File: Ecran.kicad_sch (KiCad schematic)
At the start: 0 parts

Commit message: Test ajout de composant depuis l'internet
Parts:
- added U3: 8205A, 8205A:SOT95P285X140-6N, symbol 8205A:8205A
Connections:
- new net: U3.2, U3.5
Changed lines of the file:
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@@
 	(generator_version "9.0")
 	(paper "A4")
+	(symbol
+		(lib_id "8205A:8205A")
+		(at 81.28 81.28 0)
+		(unit 1)
+		(exclude_from_sim no)
+		(in_bom yes)
+		(on_board yes)
+		(dnp no)
+		(fields_autoplaced yes)
+		(property "Reference" "U3"
+			(at 90.17 79.0828 0)
+			(effects
+				(font
+					(size 1.27 1.27)
+				)
+				(justify left)
+			)
+		)
+		(property "Value" "8205A"
+			(at 90.17 81.6228 0)
+			(effects
+				(font
+					(size 1.27 1.27)
+				)
+				(justify left)
+			)
+		)
+		(property "Footprint" "8205A:SOT95P285X140-6N"
+			(at 81.28 81.28 0)
+			(effects
+				(font
+					(size 1.27 1.27)
+				)
+				(justify bottom)
+				(hide yes)
+			)
+		)
+		(property "Datasheet" ""
+			(at 81.28 81.28 0)
+			(effects
+				(font
+					(size 1.27 1.27)
+				)
+				(hide yes)
+			)
+		)
+		(property "Description" ""
+			(at 81.28 81.28 0)
+			(effects
+				(font
+					(size 1.27 1.27)
+				)
+				(hide yes)
+			)
+		)
+		(property "MF" "UMW"
+			(at 81.28 81.28 0)
+			(effects
+				(font
+					(size 1.27 1.27)
+				)
+				(justify bottom)
+				(hide yes)
+			)
+		)
+		(property "MAXIMUM_PACKAGE_HEIGHT" "1.40mm"
+			(at 81.28 81.28 0)
+			(effects
+				(font
+					(size 1.27 1.27)
+				)
+				(justify bottom)
+				(hide yes)
+			)
+		)
+		(property "Package" "SOT-23-6 UMW"
+			(at 81.28 81.28 0)
+			(effects
+				(font
+					(size 1.27 1.27)
+				)
+				(justify bottom)
+				(hide yes)
+			)
+		)
+		(property "Price" "None"
+			(at 81.28 81.28 0)
+			(effects
+				(font
+					(size 1.27 1.27)
+				)
+				(justify bottom)
+				(hide yes)
+			)
+		)
+		(property "Check_prices" "https://www.snapeda.com/parts/8205A/UMW/view-part/?ref=eda"
+			(at 81.28 81.28 0)
+			(effects
+				(font
+					(size 1.27 1.27)
+				)
+				(justify bottom)
+				(hide yes)
+			)
+		)
+		(property "STANDARD" "IPC 7351B"
+			(at 81.28 81.28 0)
+			(effects
+				(font
+					(size 1.27 1.27)
+				)
+				(justify bottom)
+				(hide yes)
+			)
+		)
+		(property "PARTREV" "NA"
+			(at 81.28 81.28 0)
+			(effects
+				(font
+					(size 1.27 1.27)
+				)
+				(justify bottom)
+				(hide yes)
+			)
+		)
+		(property "SnapEDA_Link" "https://www.snapeda.com/parts/8205A/UMW/view-part/?ref=snap"
+			(at 81.28 81.28 0)
+			(effects
+				(font
+					(size 1.27 1.27)
+				)
+				(justify bottom)
+				(hide yes)
+			)
+		)
+		(property "MP" "8205A"
+			(at 81.28 81.28 0)
+			(effects
+				(font
+					(size 1.27 1.27)
+				)
+				(justify bottom)
+				(hide yes)
+			)
+		)
+		(property "Description_1" "Mosfet Array 20V 5A 830mW (Ta) Surface Mount SOT-23-6"
+			(at 81.28 81.28 0)
+			(effects
+				(font
+					(size 1.27 1.27)
+				)
+				(justify bottom)
+				(hide yes)
+			)
+		)
+		(property "Availability" "In Stock"
+			(at 81.28 81.28 0)
+			(effects
+				(font
+					(size 1.27 1.27)
+				)
+				(justify bottom)
+				(hide yes)
+			)
+		)
+		(property "MANUFACTURER" "UMW"
+			(at 81.28 81.28 0)
+			(effects
+				(font
+					(size 1.27 1.27)
+				)
+				(justify bottom)
+				(hide yes)
+			)
+		)
+		(pin "6"
+		)
+		(pin "3"
+		)
+		(pin "1"
+		)
+		(pin "4"
+		)
+		(pin "2"
+		)
+		(pin "5"
+		)
+		(instances
+			(project ""
+				(path "/90bd0b60-6e70-43e1-8410-99fb54688c17/3922ef04-1be0-4a1a-a432-baea08402c76"
+					(reference "U3")
+					(unit 1)
+				)
+			)
+		)
+	)
 )

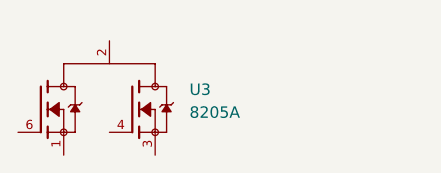
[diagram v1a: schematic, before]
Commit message: Correction capteur + ajout composant
Il fallait changer le nom dans le gestionnaire de footprint
Correction de la connectique du capteur, mais à vérifier quand même
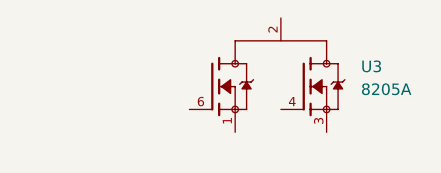
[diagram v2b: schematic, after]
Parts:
- U3: footprint 8205A:SOT95P285X140-6N -> Composants_Perso:SOT95P285X140-6N
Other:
- moved on the sheet: U3
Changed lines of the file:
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@@
 	(symbol
 		(lib_id "8205A:8205A")
-		(at 81.28 81.28 0)
+		(at 100.33 78.74 0)
 		(unit 1)
 		(exclude_from_sim no)
@@
 		(fields_autoplaced yes)
 		(property "Reference" "U3"
-			(at 90.17 79.0828 0)
+			(at 109.22 76.5428 0)
 			(effects
 				(font
@@
 		)
 		(property "Value" "8205A"
-			(at 90.17 81.6228 0)
+			(at 109.22 79.0828 0)
 			(effects
 				(font
@@
 			)
 		)
-		(property "Footprint" "8205A:SOT95P285X140-6N"
-			(at 81.28 81.28 0)
+		(property "Footprint" "Composants_Perso:SOT95P285X140-6N"
+			(at 100.33 78.74 0)
 			(effects
 				(font
@@
 		)
 		(property "Datasheet" ""
-			(at 81.28 81.28 0)
+			(at 100.33 78.74 0)
 			(effects
 				(font
@@
 		)
 		(property "Description" ""
-			(at 81.28 81.28 0)
+			(at 100.33 78.74 0)
 			(effects
 				(font
@@
 		)
 		(property "MF" "UMW"
-			(at 81.28 81.28 0)
+			(at 100.33 78.74 0)
 			(effects
 				(font
@@
 		)
 		(property "MAXIMUM_PACKAGE_HEIGHT" "1.40mm"
-			(at 81.28 81.28 0)
+			(at 100.33 78.74 0)
 			(effects
 				(font
@@
 		)
 		(property "Package" "SOT-23-6 UMW"
-			(at 81.28 81.28 0)
+			(at 100.33 78.74 0)
 			(effects
 				(font
@@
 		)
 		(property "Price" "None"
-			(at 81.28 81.28 0)
+			(at 100.33 78.74 0)
 			(effects
 				(font
@@
 		)
 		(property "Check_prices" "https://www.snapeda.com/parts/8205A/UMW/view-part/?ref=eda"
-			(at 81.28 81.28 0)
+			(at 100.33 78.74 0)
 			(effects
 				(font
@@
 		)
 		(property "STANDARD" "IPC 7351B"
-			(at 81.28 81.28 0)
+			(at 100.33 78.74 0)
 			(effects
 				(font
@@
 		)
 		(property "PARTREV" "NA"
-			(at 81.28 81.28 0)
+			(at 100.33 78.74 0)
 			(effects
 				(font
@@
 		)
 		(property "SnapEDA_Link" "https://www.snapeda.com/parts/8205A/UMW/view-part/?ref=snap"
-			(at 81.28 81.28 0)
+			(at 100.33 78.74 0)
 			(effects
 				(font
@@
 		)
 		(property "MP" "8205A"
-			(at 81.28 81.28 0)
+			(at 100.33 78.74 0)
 			(effects
 				(font
@@
 		)
 		(property "Description_1" "Mosfet Array 20V 5A 830mW (Ta) Surface Mount SOT-23-6"
-			(at 81.28 81.28 0)
+			(at 100.33 78.74 0)
 			(effects
 				(font
@@
 		)
 		(property "Availability" "In Stock"
-			(at 81.28 81.28 0)
+			(at 100.33 78.74 0)
 			(effects
 				(font
@@
 		)
 		(property "MANUFACTURER" "UMW"
-			(at 81.28 81.28 0)
+			(at 100.33 78.74 0)
 			(effects
 				(font

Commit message: Partie écran
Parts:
- removed U3: 8205A, Composants_Perso:SOT95P285X140-6N, symbol 8205A:8205A
- added C10, C11, C12, C14, C6, C7, C8, C9: 1uF/50V, symbol Device:C_Small
- added C3, C4: 4.7uF/25V, symbol Device:C
- added C5: 100nF/50V, symbol Device:C
- added D1, D2, D3: MBR0530, Diode_SMD:D_SOD-123, symbol Diode:MBR0530
- added J1: Conn_01x24_Pin, symbol Connector:Conn_01x24_Pin
- added L1: 10u, symbol Device:L
- added Q1: Q_NMOS_GSD, symbol Transistor_FET:Q_NMOS_GSD
- added Q2: Q_NPN_BCE, symbol Transistor_BJT:Q_NPN_BCE
- added R3: 3, symbol Device:R
- added R4: 10K, symbol Device:R
- added R5: 100k, symbol Device:R
- added R6: 10k, symbol Device:R
- added R7: 47K, symbol Device:R
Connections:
- new net: C3.2, D3.2 (A), L1.2, Q1.3 (D)
- new net: C3.1, D1.2 (A), D2.1 (K)
- new net: Q2.1 (B), R5.1, R6.2
- new net: C11.1, J1.24 (Pin_24)
- new net: C10.1, J1.22 (Pin_22)
- new net: C8.1, J1.18 (Pin_18)
- new net: C12.1, J1.5 (Pin_5)
- new net: C14.1, J1.20 (Pin_20)
- new net: Q2.2 (C), R7.1
- new net 3V3_OUT: C4.2, C6.1, J1.15 (Pin_15), J1.16 (Pin_16), L1.1
- new net BS: J1.8 (Pin_8)
- new net EPD PWR: R6.1
- new net EPD_BUSY: J1.9 (Pin_9)
- new net EPD_CS: J1.12 (Pin_12)
- new net EPD_DC: J1.11 (Pin_11)
- new net EPD_DIN: J1.14 (Pin_14)
- new net EPD_RST: J1.10 (Pin_10)
- new net EPD_SCK: J1.13 (Pin_13)
- new net GDR: J1.2 (Pin_2), Q1.1 (G), R4.2
- new net GND: C10.2, C11.2, C12.2, C14.2, C4.1, C5.2, C6.2, C7.2, C8.2, C9.2, D1.1 (K), J1.17 (Pin_17), Q2.3 (E), R3.1, R4.1, R5.2
- new net RESE: J1.3 (Pin_3), Q1.2 (S), R3.2
- new net VCC INT: C5.1, R7.2
- new net VGH: C9.1, D3.1 (K), J1.21 (Pin_21)
- new net VGL: C7.1, D2.2 (A), J1.23 (Pin_23)
- no-connect marks 0 -> 5
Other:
- note added: "Boost Converter"
- note added: "Connecteur"
- note added: "Interrupteur de puissance"

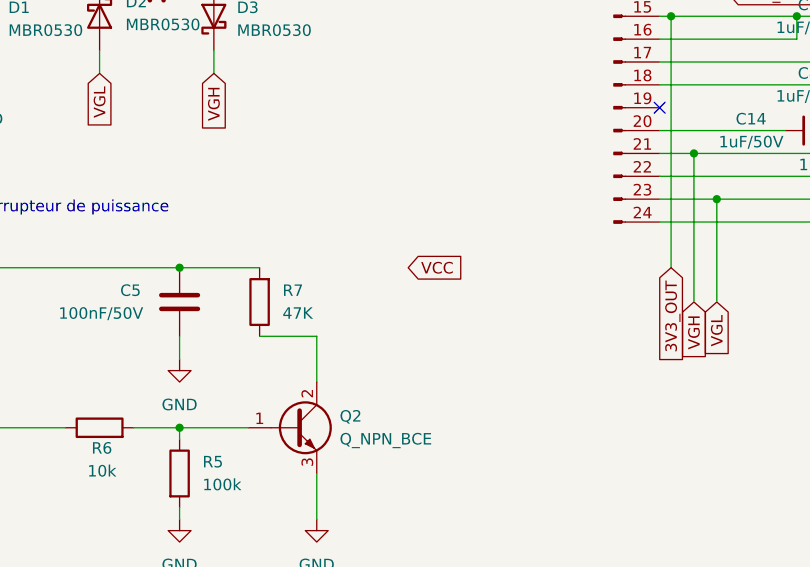
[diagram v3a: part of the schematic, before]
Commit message: Ajout total de la partie alimentation
Ajout de composant depuis un site internet ->OK
Fin de la partie écran et alimentation : ajout de tous les composants
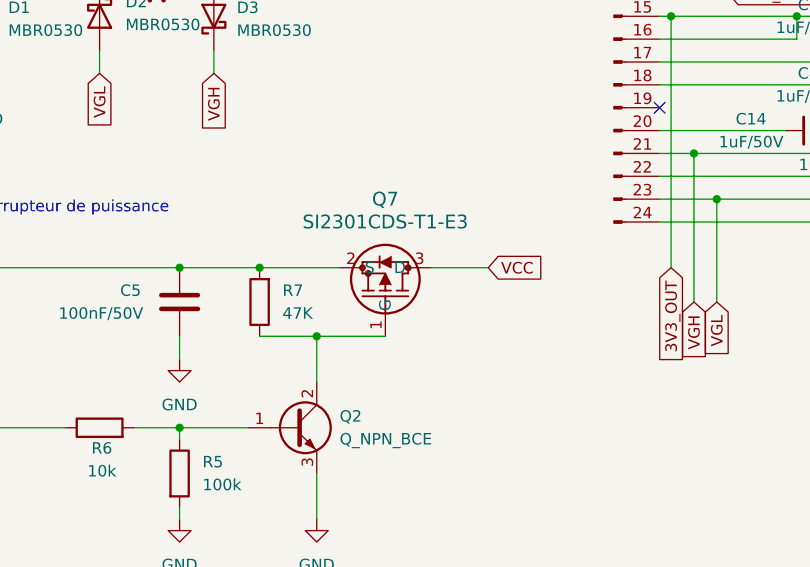
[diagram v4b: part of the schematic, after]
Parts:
- added Q7: SI2301CDS-T1-E3, Composants_Perso:SI2301CDS_T1_E3, symbol SI2301CDS_T1_E3:SI2301CDS-T1-E3
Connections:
- net VCC: now also Q7.3 (D)
- net VCC INT: now also Q7.2 (S)
- net at Q2.2 (C), R7.1: now also Q7.1 (G)
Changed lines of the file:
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@@
 	)
 	(junction
+		(at 76.2 92.71)
+		(diameter 0)
+		(color 0 0 0 0)
+	)
+	(junction
 		(at 38.1 38.1)
 		(diameter 0)
@@
 	)
 	(junction
+		(at 82.55 100.33)
+		(diameter 0)
+		(color 0 0 0 0)
+	)
+	(junction
 		(at 179.07 69.85)
 		(diameter 0)
@@
 	(wire
 		(pts
+			(xy 76.2 92.71) (xy 85.09 92.71)
+		)
+		(stroke
+			(width 0)
+			(type default)
+		)
+	)
+	(wire
+		(pts
 			(xy 71.12 26.67) (xy 71.12 33.02)
 		)
@@
 	(wire
 		(pts
-			(xy 82.55 100.33) (xy 82.55 105.41)
+			(xy 82.55 100.33) (xy 90.17 100.33)
 		)
 		(stroke
@@
 	(wire
 		(pts
-			(xy 59.69 38.1) (xy 63.5 38.1)
+			(xy 76.2 100.33) (xy 82.55 100.33)
 		)
 		(stroke
@@
 	(wire
 		(pts
-			(xy 76.2 100.33) (xy 82.55 100.33)
+			(xy 59.69 38.1) (xy 63.5 38.1)
 		)
 		(stroke
@@
 	(wire
 		(pts
+			(xy 95.25 92.71) (xy 101.6 92.71)
+		)
+		(stroke
+			(width 0)
+			(type default)
+		)
+	)
+	(wire
+		(pts
 			(xy 120.65 87.63) (xy 172.72 87.63)
 		)
@@
 	(wire
 		(pts
+			(xy 82.55 105.41) (xy 82.55 100.33)
+		)
+		(stroke
+			(width 0)
+			(type default)
+		)
+	)
+	(wire
+		(pts
 			(xy 120.65 54.61) (xy 128.27 54.61)
 		)
@@
 	(global_label "VCC"
 		(shape input)
-		(at 92.71 92.71 0)
+		(at 101.6 92.71 0)
 		(fields_autoplaced yes)
 		(effects
@@
 		)
 		(property "Intersheetrefs" "${INTERSHEET_REFS}"
-			(at 99.3238 92.71 0)
+			(at 108.2138 92.71 0)
 			(effects
 				(font
@@
 					(unit 1)
 				)
+			)
+		)
+	)
+	(symbol
+		(lib_id "SI2301CDS_T1_E3:SI2301CDS-T1-E3")
+		(at 90.17 100.33 270)
+		(mirror x)
+		(unit 1)
+		(exclude_from_sim no)
+		(in_bom yes)
+		(on_board yes)
+		(dnp no)
+		(property "Reference" "Q7"
+			(at 90.17 85.09 90)
+			(effects
+				(font
+					(size 1.524 1.524)
+				)
+			)
+		)
+		(property "Value" "SI2301CDS-T1-E3"
+			(at 90.17 87.63 90)
+			(effects
+				(font
+					(size 1.524 1.524)
+				)
+			)
+		)
+		(property "Footprint" "Composants_Perso:SI2301CDS_T1_E3"
+			(at 90.17 100.33 0)
+			(effects
+				(font
+					(size 1.27 1.27)
+					(italic yes)
+				)
+				(hide yes)
+			)
+		)
+		(property "Datasheet" "https://www.vishay.com/doc?68741"
+			(at 90.17 100.33 0)
+			(effects
+				(font
+					(size 1.27 1.27)
+					(italic yes)
+				)
+				(hide yes)
+			)
+		)
+		(property "Description" ""
+			(at 90.17 100.33 0)
+			(effects
+				(font
+					(size 1.27 1.27)
+				)
+				(hide yes)
+			)
+		)
+		(pin "1"
+		)
+		(pin "3"
+		)
+		(pin "2"
+		)
+		(instances
+			(project ""
+				(path "/90bd0b60-6e70-43e1-8410-99fb54688c17/3922ef04-1be0-4a1a-a432-baea08402c76"
+					(reference "Q7")
+					(unit 1)
+				)

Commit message: Dernieres pour review
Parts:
- removed C5: 100nF/50V, symbol Device:C
- removed Q2: Q_NPN_BCE, symbol Transistor_BJT:Q_NPN_BCE
- removed Q7: SI2301CDS-T1-E3, Composants_Perso:SI2301CDS_T1_E3, symbol SI2301CDS_T1_E3:SI2301CDS-T1-E3
- removed R5: 100k, symbol Device:R
- removed R6: 10k, symbol Device:R
- removed R7: 47K, symbol Device:R
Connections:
- net BS: no longer names the net of J1.8 (Pin_8)
- no-connect marks 5 -> 6
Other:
- note removed: "Interrupteur de puissance"
- moved on the sheet: C3, C4, D1, D2, D3, L1, Q1, R3, R4

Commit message: revue schema
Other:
- note added: "pin 8 à la masse"
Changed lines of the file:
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@@
+		)
+	)
+	(text "pin 8 à la masse"
+		(exclude_from_sim no)
+		(at 130.556 46.482 0)
+		(effects
+			(font
+				(size 1.27 1.27)
+				(color 255 0 0 1)
+			)
 		)
 	)

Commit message: premieres modif depuis la review
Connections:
- net GND: now also J1.8 (Pin_8)
- no-connect marks 6 -> 5
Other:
- note removed: "pin 8 à la masse"
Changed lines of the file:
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@@
-		)
-	)
-	(text "pin 8 à la masse"
-		(exclude_from_sim no)
-		(at 130.556 46.482 0)
-		(effects
-			(font
-				(size 1.27 1.27)
-				(color 255 0 0 1)
-			)
 		)
 	)
@@
 	)
 	(junction
+		(at 179.07 46.99)
+		(diameter 0)
+		(color 0 0 0 0)
+	)
+	(junction
 		(at 124.46 80.01)
 		(diameter 0)
@@
 	)
 	(no_connect
-		(at 120.65 46.99)
-	)
-	(no_connect
 		(at 120.65 74.93)
 	)
@@
 	(wire
 		(pts
+			(xy 179.07 46.99) (xy 179.07 64.77)
+		)
+		(stroke
+			(width 0)
+			(type default)
+		)
+	)
+	(wire
+		(pts
 			(xy 146.05 39.37) (xy 179.07 39.37)
 		)
@@
 	(wire
 		(pts
+			(xy 120.65 46.99) (xy 179.07 46.99)
+		)
+		(stroke
+			(width 0)
+			(type default)
+		)
+	)
+	(wire
+		(pts
 			(xy 179.07 69.85) (xy 179.07 72.39)
 		)
@@
 	(wire
 		(pts
-			(xy 179.07 39.37) (xy 179.07 64.77)
-		)
-		(stroke
+			(xy 179.07 39.37) (xy 179.07 46.99)
+		)
+		(stroke
